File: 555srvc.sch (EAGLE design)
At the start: 10 parts, among them IC1 555

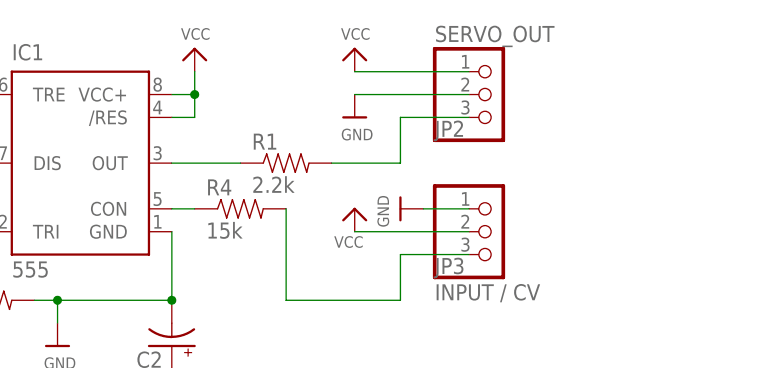
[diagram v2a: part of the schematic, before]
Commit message: changes pintout to coform with servo out.
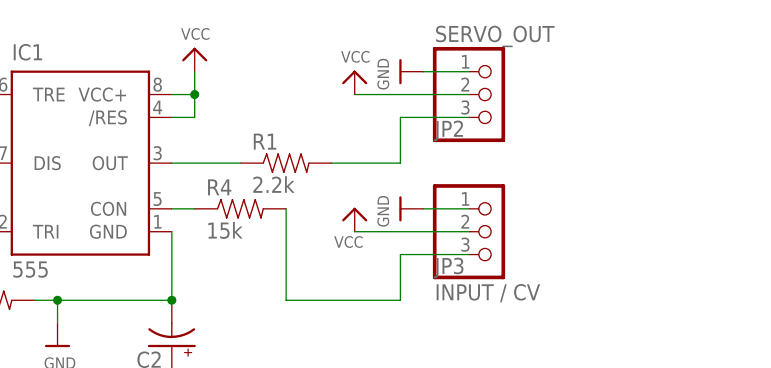
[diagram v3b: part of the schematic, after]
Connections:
- net GND: now also JP2.1; no longer JP2.2
- net VCC: now also JP2.2; no longer JP2.1
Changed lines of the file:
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@@
 <attribute name="VALUE" x="42.418" y="39.751" size="1.778" layer="96"/>
 </instance>
-<instance part="P+5" gate="VCC" x="86.36" y="71.12"/>
-<instance part="U$3" gate="G$1" x="86.36" y="63.5"/>
+<instance part="P+5" gate="VCC" x="86.36" y="68.58"/>
+<instance part="U$3" gate="G$1" x="91.44" y="68.58" rot="R270"/>
 <instance part="JP2" gate="A" x="101.6" y="66.04" smashed="yes">
 <attribute name="NAME" x="95.25" y="61.341" size="1.778" layer="95"/>
@@
 </segment>
 <segment>
-<pinref part="P+5" gate="VCC" pin="VCC"/>
-<wire x1="99.06" y1="68.58" x2="86.36" y2="68.58" width="0.1524" layer="91"/>
-<pinref part="JP2" gate="A" pin="1"/>
-</segment>
-<segment>
 <pinref part="P+3" gate="VCC" pin="VCC"/>
 <wire x1="66.04" y1="33.02" x2="66.04" y2="35.56" width="0.1524" layer="91"/>
@@
 <wire x1="99.06" y1="50.8" x2="86.36" y2="50.8" width="0.1524" layer="91"/>
 </segment>
-</net>
-<net name="GND" class="0">
 <segment>
-<pinref part="U$3" gate="G$1" pin="GND"/>
+<pinref part="P+5" gate="VCC" pin="VCC"/>
 <pinref part="JP2" gate="A" pin="2"/>
 <wire x1="86.36" y1="66.04" x2="99.06" y2="66.04" width="0.1524" layer="91"/>
 </segment>
+</net>
+<net name="GND" class="0">
 <segment>
 <pinref part="IC1" gate="G$1" pin="GND"/>
@@
 <wire x1="93.98" y1="53.34" x2="99.06" y2="53.34" width="0.1524" layer="91"/>
 </segment>
+<segment>
+<pinref part="U$3" gate="G$1" pin="GND"/>
+<pinref part="JP2" gate="A" pin="1"/>
+<wire x1="93.98" y1="68.58" x2="99.06" y2="68.58" width="0.1524" layer="91"/>
+</segment>
 </net>

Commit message: attiny85 ver
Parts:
- removed D1: (no value), 555srvc:DIODESOD-123
- removed IC1: 555, 555srvc:NE555D
- removed JP3: INPUT / CV, 555srvc:PINHD-1X3CB
- removed R1: 2.2k, 555srvc:RESISTOR0805-RES
- removed R2: 1.5k, 555srvc:RESISTOR0805-RES
- removed R3: 47k, 555srvc:RESISTOR0805-RES
- removed R4: 15k, 555srvc:RESISTOR0805-RES
- added JP1: SERVO_OUT01, 555srvc:PINHD-1X3CB
- added JP4: power-input, ATtami:HEADER-1X4ROUND
- added U1: ATTINY85-20SU, ATtami:ATTINY85-20SU
- C2: value (none) -> 1000uF
- JP2: value SERVO_OUT -> SERVO_OUT02
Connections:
- removed net INPUT: JP3.3, R4.2
- removed net N$1: C1.1, D1.C, IC1.TRE, IC1.TRI, R3.1
- removed net N$2: D1.A, IC1.DIS, R2.2, R3.2
- removed net N$4: IC1.CON, R4.1
- removed net N$5: IC1.OUT, R1.1
- removed net SERVO_OUT: JP2.3, R1.2
- new net IN01: JP4.3
- new net IN02: JP4.4
- new net SRV01: JP1.3, U1.PB1
- new net SRV02: JP2.3, U1.PB4
- net GND: now also C1.1, JP1.2, JP2.2, JP4.2, U1.GND; no longer C1.2, IC1.GND, JP2.1, JP3.1
- net VCC: now also C1.2, JP1.1, JP2.1, JP4.1, U1.VCC; no longer IC1./RES, IC1.VCC+, JP2.2, JP3.2, R2.1
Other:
- moved on the sheet: C1, C2, JP2
